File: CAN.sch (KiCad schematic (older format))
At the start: 17 parts, among them J10 CAN_Out, U10 ADM3055E, U11 CDSOT23-T24CAN

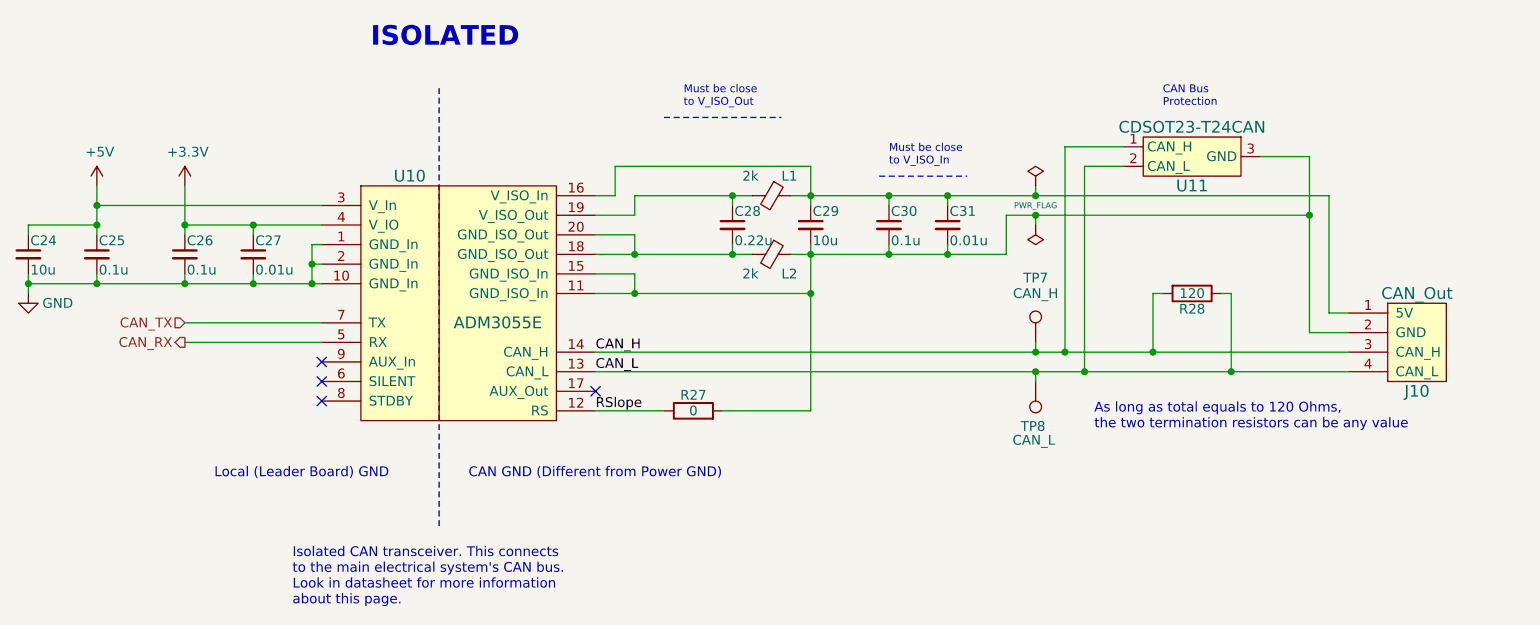
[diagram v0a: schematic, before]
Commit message: Updates BAS70-04 footprint for Contactor auxillary interface
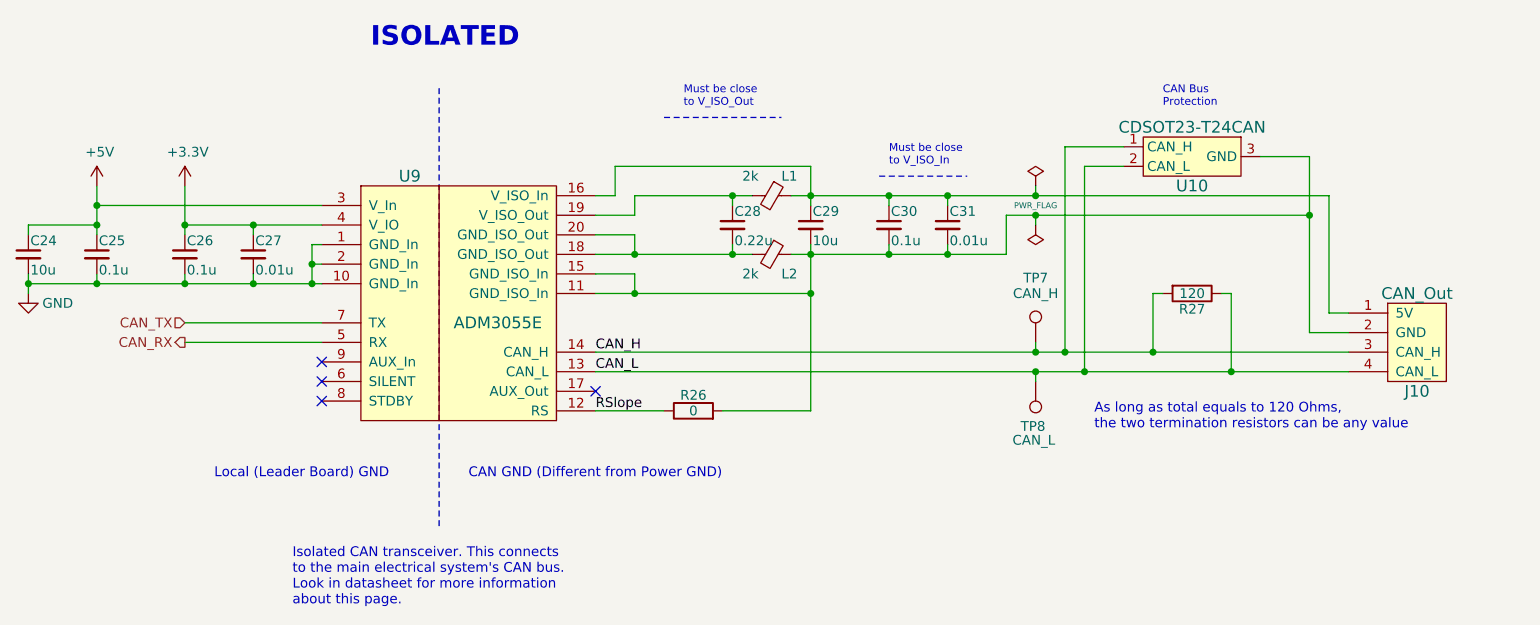
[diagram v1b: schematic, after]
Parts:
- renumbered R27 to R26, R28 to R27, U11 to U10, U10 to U9
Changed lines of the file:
@@
 $EndComp
 $Comp
-L Device:R R28
+L Device:R R27
 U 1 1 5C2B4301
 P 8100 3550
-F 0 "R28" V 8180 3550 50  0000 C CNN
+F 0 "R27" V 8180 3550 50  0000 C CNN
 F 1 "120" V 8100 3550 50  0000 C CNN
 F 2 "Resistor_SMD:R_0805_2012Metric" V 8030 3550 50  0001 C CNN
@@
 $EndComp
 $Comp
-L utsvt-chips:ADM3055E U10
+L utsvt-chips:ADM3055E U9
 U 1 1 5C2B4359
 P 4350 3600
-F 0 "U10" H 4100 4250 60  0000 C CNN
+F 0 "U9" H 4100 4250 60  0000 C CNN
 F 1 "ADM3055E" H 4550 3500 60  0000 C CNN
 F 2 "UTSVT_ICs:SOIC-20W_7.5x15.4mm_Pitch1.27mm" H 4350 3700 60  0001 C CNN
@@
 $EndComp
 $Comp
-L utsvt-chips:CDSOT23-T24CAN U11
+L utsvt-chips:CDSOT23-T24CAN U10
 U 1 1 5C2B43A0
 P 8100 2850
-F 0 "U11" H 8100 2700 60  0000 C CNN
+F 0 "U10" H 8100 2700 60  0000 C CNN
 F 1 "CDSOT23-T24CAN" H 8100 3000 60  0000 C CNN
 F 2 "Package_TO_SOT_SMD:SOT-23W" H 8100 2850 60  0001 C CNN
@@
 $EndComp
 $Comp
-L Device:R R27
+L Device:R R26
 U 1 1 5C2B43C4
 P 5550 4150
-F 0 "R27" V 5630 4150 50  0000 C CNN
+F 0 "R26" V 5630 4150 50  0000 C CNN
 F 1 "0" V 5550 4150 50  0000 C CNN
 F 2 "Resistor_SMD:R_0805_2012Metric" V 5480 4150 50  0001 C CNN
@@
 	5250 3050 5250 3150
 $Comp
-L power:GND #PWR062
+L power:GND #PWR064
 U 1 1 5C28BDDE
 P 2150 3550
-F 0 "#PWR062" H 2150 3300 50  0001 C CNN
+F 0 "#PWR064" H 2150 3300 50  0001 C CNN
 F 1 "GND" H 2300 3500 50  0000 C CNN
 F 2 "" H 2150 3550 50  0001 C CNN
@@
 	2500 3000 2500 3100
 $Comp
-L power:+3.3V #PWR064
+L power:+3.3V #PWR066
 U 1 1 5C4ABE05
 P 2950 3000
-F 0 "#PWR064" H 2950 2850 50  0001 C CNN
+F 0 "#PWR066" H 2950 2850 50  0001 C CNN
 F 1 "+3.3V" H 2965 3173 50  0000 C CNN
 F 2 "" H 2950 3000 50  0001 C CNN
@@
 	2950 3000 2950 3200
 $Comp
-L power:+5V #PWR063
+L power:+5V #PWR065
 U 1 1 5C4C2AB0
 P 2500 3000
-F 0 "#PWR063" H 2500 2850 50  0001 C CNN
+F 0 "#PWR065" H 2500 2850 50  0001 C CNN
 F 1 "+5V" H 2515 3173 50  0000 C CNN
 F 2 "" H 2500 3000 50  0001 C CNN
